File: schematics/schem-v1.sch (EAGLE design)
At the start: 13 parts, among them Q1 TIP120

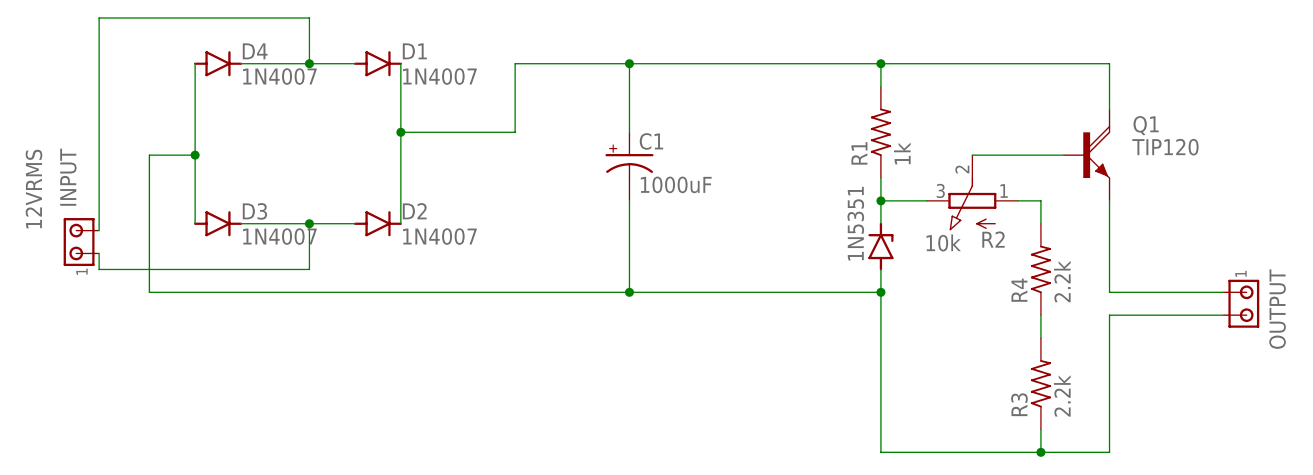
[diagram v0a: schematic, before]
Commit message: second iteration: transformer adjustments
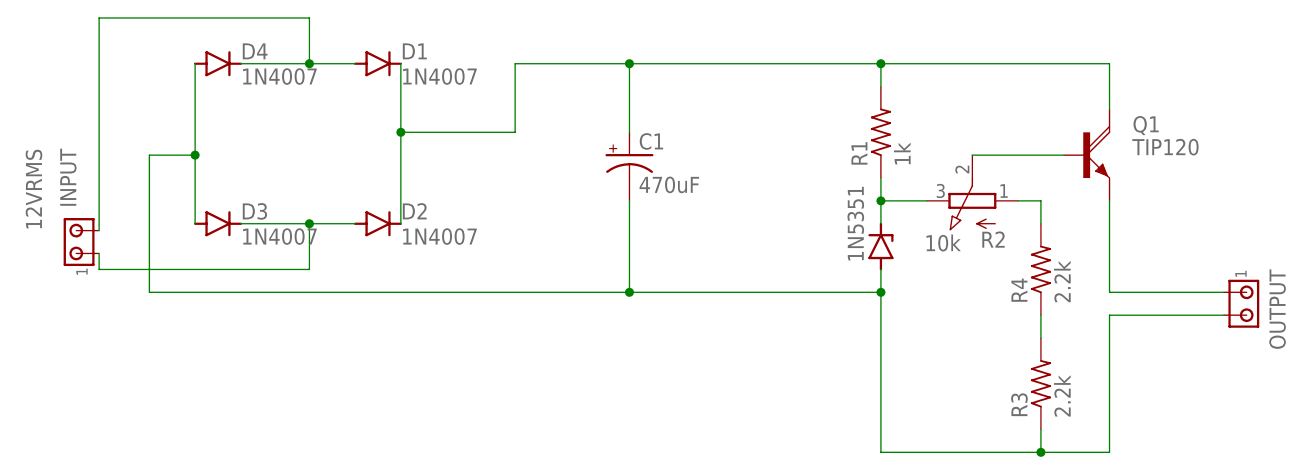
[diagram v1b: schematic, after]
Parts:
- C1: value 1000uF -> 470uF; device rcl:CPOL-USE5-13 -> rcl:CPOL-USE3.5-10
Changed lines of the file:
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@@
 <part name="D3" library="diode" library_urn="urn:adsk.eagle:library:210" deviceset="1N4004" device="" package3d_urn="urn:adsk.eagle:package:43336/1" value="1N4007"/>
 <part name="D4" library="diode" library_urn="urn:adsk.eagle:library:210" deviceset="1N4004" device="" package3d_urn="urn:adsk.eagle:package:43336/1" value="1N4007"/>
-<part name="C1" library="rcl" library_urn="urn:adsk.eagle:library:334" deviceset="CPOL-US" device="E5-13" package3d_urn="urn:adsk.eagle:package:23375/1" value="1000uF"/>
 <part name="R1" library="rcl" library_urn="urn:adsk.eagle:library:334" deviceset="R-US_" device="0207/10" package3d_urn="urn:adsk.eagle:package:23491/2" value="1k"/>
 <part name="1N5351" library="diode" library_urn="urn:adsk.eagle:library:210" deviceset="ZENER-DIODE" device="DO41Z10" package3d_urn="urn:adsk.eagle:package:43341/1"/>
@@
 <part name="Q1" library="transistor-power" library_urn="urn:adsk.eagle:library:400" deviceset="TIP120" device="" package3d_urn="urn:adsk.eagle:package:29488/1"/>
 <part name="OUTPUT" library="con-amp" library_urn="urn:adsk.eagle:library:127" deviceset="MTA02-100" device="" package3d_urn="urn:adsk.eagle:package:8081649/1"/>
+<part name="C1" library="rcl" library_urn="urn:adsk.eagle:library:334" deviceset="CPOL-US" device="E3.5-10" package3d_urn="urn:adsk.eagle:package:23351/1" value="470uF"/>
 </parts>
 <sheets>
@@
 <attribute name="NAME" x="17.78" y="74.1426" size="1.778" layer="95"/>
 <attribute name="VALUE" x="17.78" y="71.3486" size="1.778" layer="96"/>
-</instance>
-<instance part="C1" gate="G$1" x="60.96" y="63.5" smashed="yes">
-<attribute name="NAME" x="61.976" y="64.135" size="1.778" layer="95"/>
-<attribute name="VALUE" x="61.976" y="59.309" size="1.778" layer="96"/>
 </instance>
 <instance part="R1" gate="G$1" x="88.9" y="66.04" smashed="yes" rot="R90">
@@
 <attribute name="NAME" x="132.08" y="50.8" size="1.778" layer="95" rot="R270"/>
 <attribute name="VALUE" x="125.73" y="43.18" size="1.778" layer="96" rot="R270"/>
+</instance>
+<instance part="C1" gate="G$1" x="60.96" y="63.5" smashed="yes">
+<attribute name="NAME" x="61.976" y="64.135" size="1.778" layer="95"/>
+<attribute name="VALUE" x="61.976" y="59.309" size="1.778" layer="96"/>
 </instance>
 </instances>
@@
 <wire x1="35.56" y1="66.04" x2="48.26" y2="66.04" width="0.1524" layer="91"/>
 <junction x="35.56" y="66.04"/>
-<pinref part="C1" gate="G$1" pin="+"/>
 <wire x1="60.96" y1="73.66" x2="60.96" y2="66.04" width="0.1524" layer="91"/>
 <wire x1="48.26" y1="66.04" x2="48.26" y2="73.66" width="0.1524" layer="91"/>
@@
 <pinref part="Q1" gate="1" pin="C"/>
 <wire x1="114.3" y1="73.66" x2="114.3" y2="68.58" width="0.1524" layer="91"/>
+<pinref part="C1" gate="G$1" pin="+"/>
 </segment>
 </net>
@@
 <wire x1="7.62" y1="63.5" x2="7.62" y2="48.26" width="0.1524" layer="91"/>
 <junction x="12.7" y="63.5"/>
-<pinref part="C1" gate="G$1" pin="-"/>
-<wire x1="60.96" y1="58.42" x2="60.96" y2="48.26" width="0.1524" layer="91"/>
 <wire x1="7.62" y1="48.26" x2="60.96" y2="48.26" width="0.1524" layer="91"/>
 <pinref part="1N5351" gate="G$1" pin="A"/>
+<wire x1="60.96" y1="48.26" x2="88.9" y2="48.26" width="0.1524" layer="91"/>
 <wire x1="88.9" y1="50.8" x2="88.9" y2="48.26" width="0.1524" layer="91"/>
-<wire x1="88.9" y1="48.26" x2="60.96" y2="48.26" width="0.1524" layer="91"/>
-<junction x="60.96" y="48.26"/>
 <pinref part="R3" gate="G$1" pin="1"/>
 <wire x1="106.68" y1="33.02" x2="106.68" y2="30.48" width="0.1524" layer="91"/>
@@
 <wire x1="114.3" y1="30.48" x2="106.68" y2="30.48" width="0.1524" layer="91"/>
 <junction x="106.68" y="30.48"/>
+<pinref part="C1" gate="G$1" pin="-"/>
+<wire x1="60.96" y1="58.42" x2="60.96" y2="48.26" width="0.1524" layer="91"/>
+<junction x="60.96" y="48.26"/>
 </segment>
 </net>
